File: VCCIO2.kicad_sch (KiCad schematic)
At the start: 19 parts, among them J5001 Micro_SD_Card_Det1, U3001 rv1126/rv1109

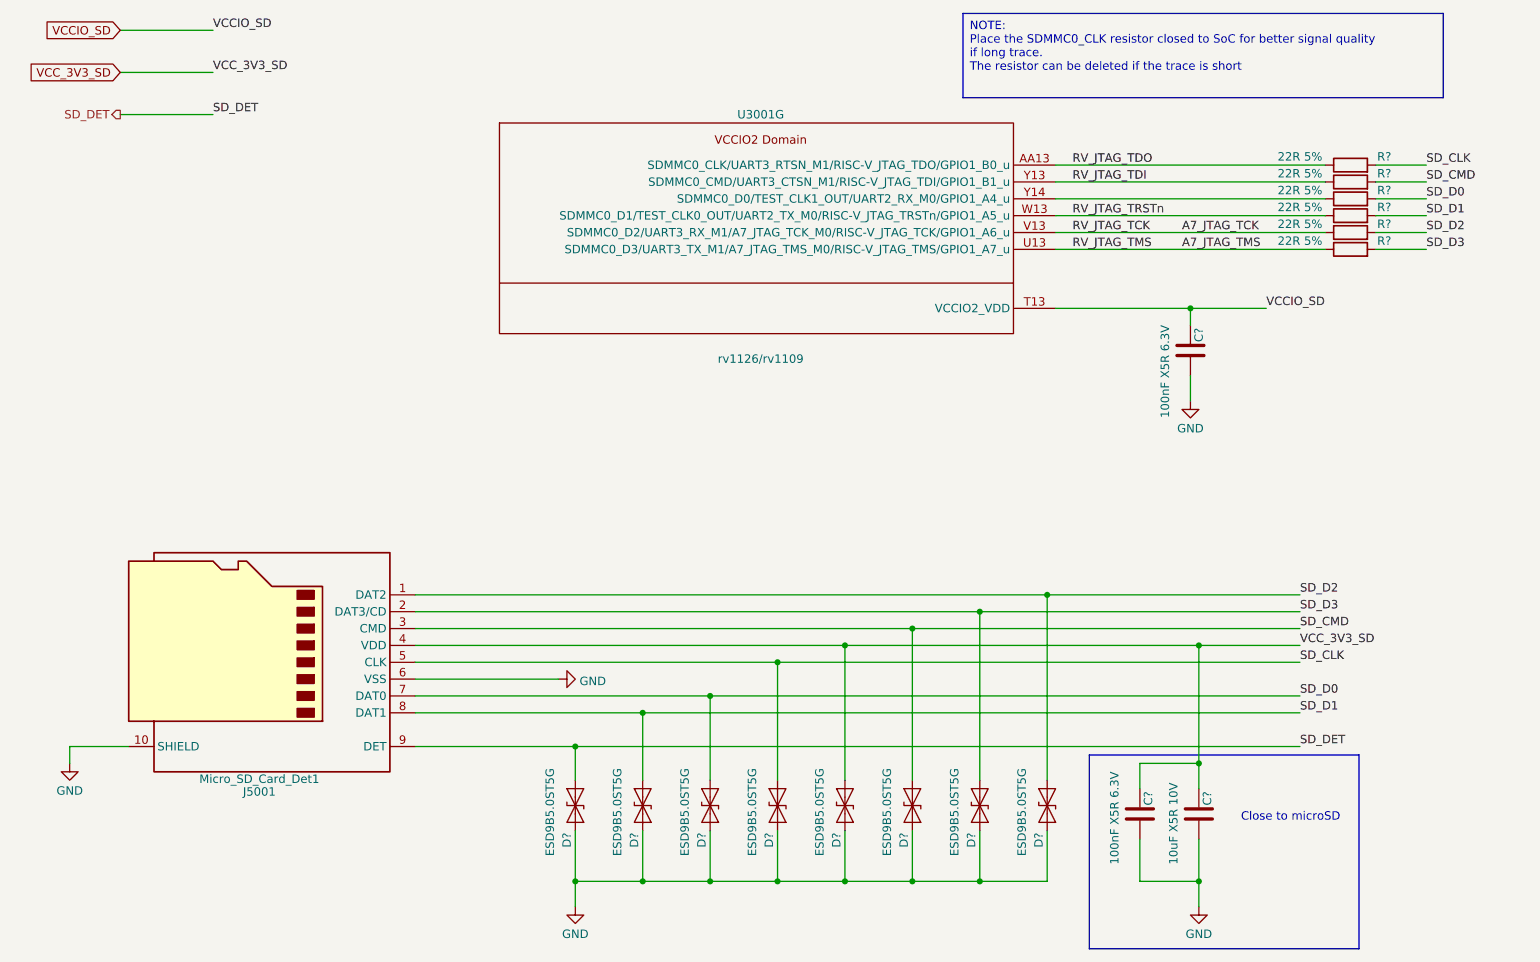
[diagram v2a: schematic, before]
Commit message: move DDR power decoupling capacitors into DDR4 Sheet
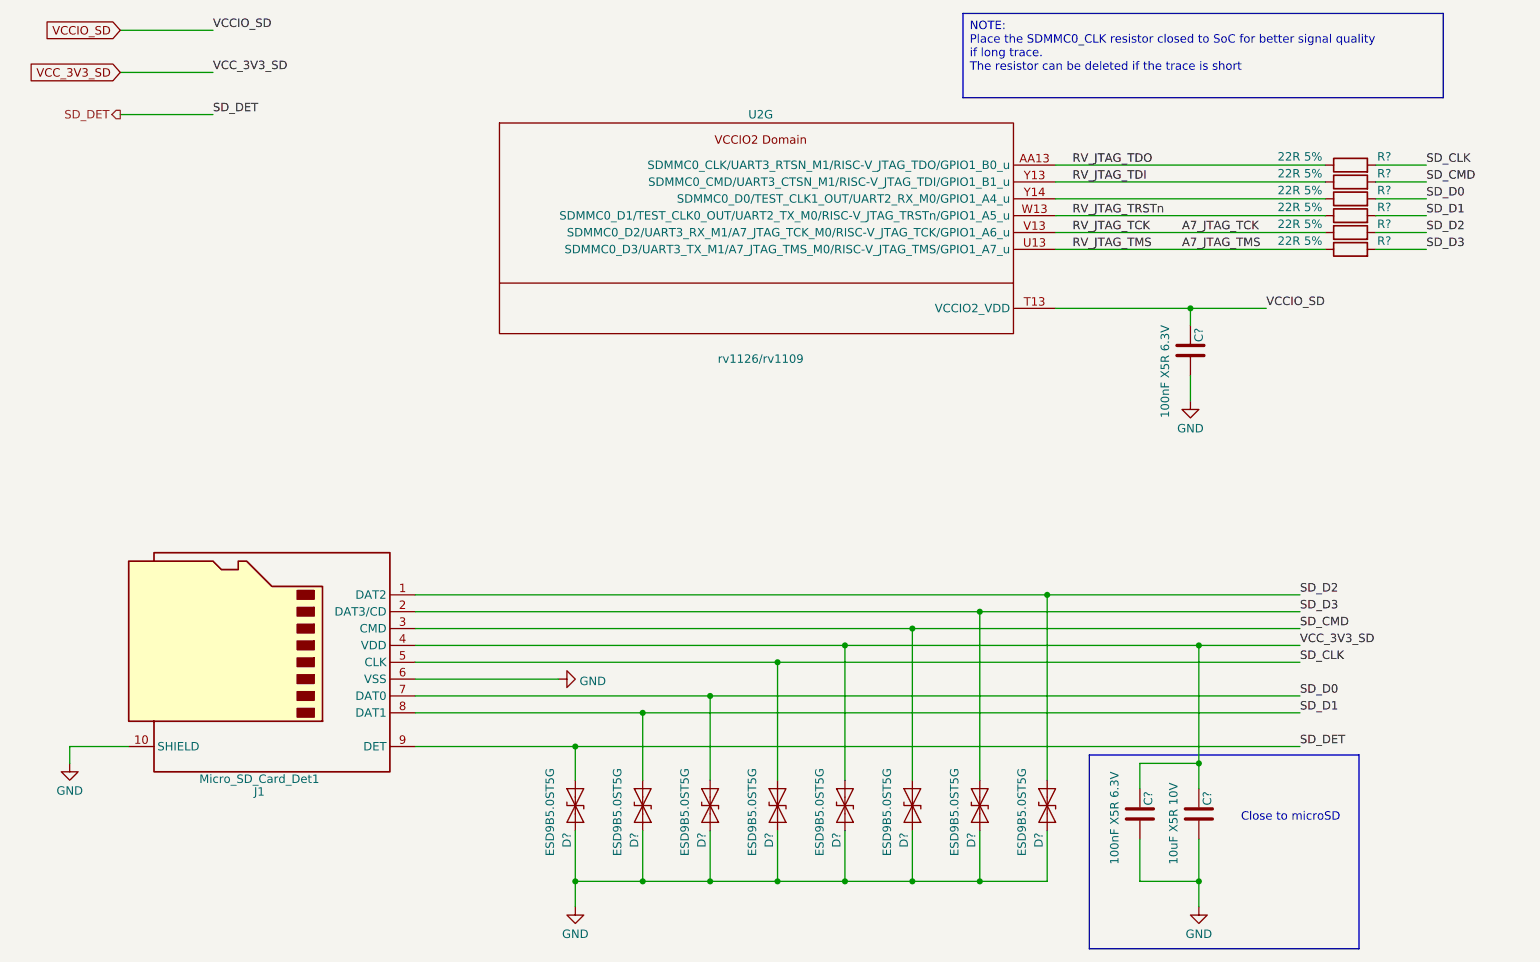
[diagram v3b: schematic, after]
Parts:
- renumbered J5001 to J1, U3001 to U2
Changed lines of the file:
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@@
         )
         (path "/e3b58043-16a3-43c8-9fad-9c9784eebfa4/4417415c-26f1-4372-988d-9fdf1c116b4b"
-          (reference "C5003") (unit 1)
+          (reference "C16") (unit 1)
         )
       )
@@
         )
         (path "/e3b58043-16a3-43c8-9fad-9c9784eebfa4/4417415c-26f1-4372-988d-9fdf1c116b4b"
-          (reference "D5003") (unit 1)
+          (reference "D3") (unit 1)
         )
       )
@@
         )
         (path "/e3b58043-16a3-43c8-9fad-9c9784eebfa4/4417415c-26f1-4372-988d-9fdf1c116b4b"
-          (reference "D5001") (unit 1)
+          (reference "D1") (unit 1)
         )
       )
@@
         )
         (path "/e3b58043-16a3-43c8-9fad-9c9784eebfa4/4417415c-26f1-4372-988d-9fdf1c116b4b"
-          (reference "C5002") (unit 1)
+          (reference "C15") (unit 1)
         )
       )
@@
   (symbol (lib_id "power:GND") (at 193.04 153.67 0) (unit 1)
     (in_bom yes) (on_board yes) (dnp no) (fields_autoplaced)
-    (property "Reference" "#PWR05005" (at 193.04 160.02 0)
+    (property "Reference" "#PWR019" (at 193.04 160.02 0)
       (effects (font (size 1.27 1.27)) hide)
     )
@@
       (project "leaf"
         (path "/e3b58043-16a3-43c8-9fad-9c9784eebfa4/4417415c-26f1-4372-988d-9fdf1c116b4b"
-          (reference "#PWR05005") (unit 1)
+          (reference "#PWR019") (unit 1)
         )
       )
@@
   (symbol (lib_id "power:GND") (at 96.52 119.38 90) (unit 1)
     (in_bom yes) (on_board yes) (dnp no) (fields_autoplaced)
-    (property "Reference" "#PWR05002" (at 102.87 119.38 0)
+    (property "Reference" "#PWR016" (at 102.87 119.38 0)
       (effects (font (size 1.27 1.27)) hide)
     )
@@
       (project "leaf"
         (path "/e3b58043-16a3-43c8-9fad-9c9784eebfa4/4417415c-26f1-4372-988d-9fdf1c116b4b"
-          (reference "#PWR05002") (unit 1)
+          (reference "#PWR016") (unit 1)
         )
       )
@@
         )
         (path "/e3b58043-16a3-43c8-9fad-9c9784eebfa4/4417415c-26f1-4372-988d-9fdf1c116b4b"
-          (reference "D5005") (unit 1)
+          (reference "D5") (unit 1)
         )
       )
@@
         )
         (path "/e3b58043-16a3-43c8-9fad-9c9784eebfa4/4417415c-26f1-4372-988d-9fdf1c116b4b"
-          (reference "D5004") (unit 1)
+          (reference "D4") (unit 1)
         )
       )
@@
         )
         (path "/e3b58043-16a3-43c8-9fad-9c9784eebfa4/4417415c-26f1-4372-988d-9fdf1c116b4b"
-          (reference "C5001") (unit 1)
+          (reference "C14") (unit 1)
         )
       )
@@
   (symbol (lib_id "Connector:Micro_SD_Card_Det1") (at 52.07 116.84 0) (mirror y) (unit 1)
     (in_bom yes) (on_board yes) (dnp no)
-    (property "Reference" "J5001" (at 51.435 136.3599 0)
+    (property "Reference" "J1" (at 51.435 136.3599 0)
       (effects (font (size 1.27 1.27)))
     )
@@
       (project "leaf"
         (path "/e3b58043-16a3-43c8-9fad-9c9784eebfa4/4417415c-26f1-4372-988d-9fdf1c116b4b"
-          (reference "J5001") (unit 1)
+          (reference "J1") (unit 1)
         )
       )
@@
         )
         (path "/e3b58043-16a3-43c8-9fad-9c9784eebfa4/4417415c-26f1-4372-988d-9fdf1c116b4b"
-          (reference "D5006") (unit 1)
+          (reference "D6") (unit 1)
         )
       )
@@
         )
         (path "/e3b58043-16a3-43c8-9fad-9c9784eebfa4/4417415c-26f1-4372-988d-9fdf1c116b4b"
-          (reference "D5008") (unit 1)
+          (reference "D8") (unit 1)
         )
       )
@@
         )
         (path "/e3b58043-16a3-43c8-9fad-9c9784eebfa4/4417415c-26f1-4372-988d-9fdf1c116b4b"
-          (reference "R5006") (unit 1)
+          (reference "R12") (unit 1)
         )
       )
@@
   (symbol (lib_id "CPU_Rockchip:rv1126_rv1109") (at 127 59.69 0) (unit 7)
     (in_bom yes) (on_board yes) (dnp no)
-    (property "Reference" "U3001" (at 127 34.29 0)
+    (property "Reference" "U2" (at 127 34.29 0)
       (effects (font (size 1.27 1.27)))
     )
@@
       (project "leaf"
         (path "/e3b58043-16a3-43c8-9fad-9c9784eebfa4/4417415c-26f1-4372-988d-9fdf1c116b4b"
-          (reference "U3001") (unit 7)
+          (reference "U2") (unit 7)
         )
       )
@@
         )
         (path "/e3b58043-16a3-43c8-9fad-9c9784eebfa4/4417415c-26f1-4372-988d-9fdf1c116b4b"
-          (reference "R5003") (unit 1)
+          (reference "R9") (unit 1)
         )
       )
@@
         )
         (path "/e3b58043-16a3-43c8-9fad-9c9784eebfa4/4417415c-26f1-4372-988d-9fdf1c116b4b"
-          (reference "D5007") (unit 1)
+          (reference "D7") (unit 1)
         )
       )
@@
         )
         (path "/e3b58043-16a3-43c8-9fad-9c9784eebfa4/4417415c-26f1-4372-988d-9fdf1c116b4b"
-          (reference "D5002") (unit 1)
+          (reference "D2") (unit 1)
         )
       )
@@
         )
         (path "/e3b58043-16a3-43c8-9fad-9c9784eebfa4/4417415c-26f1-4372-988d-9fdf1c116b4b"
-          (reference "R5005") (unit 1)
+          (reference "R11") (unit 1)
         )
       )
@@
         )
         (path "/e3b58043-16a3-43c8-9fad-9c9784eebfa4/4417415c-26f1-4372-988d-9fdf1c116b4b"
-          (reference "R5002") (unit 1)
+          (reference "R8") (unit 1)
         )
       )
@@
   (symbol (lib_id "power:GND") (at 99.06 153.67 0) (unit 1)
     (in_bom yes) (on_board yes) (dnp no) (fields_autoplaced)
-    (property "Reference" "#PWR05003" (at 99.06 160.02 0)
+    (property "Reference" "#PWR017" (at 99.06 160.02 0)
       (effects (font (size 1.27 1.27)) hide)
     )
@@
       (project "leaf"
         (path "/e3b58043-16a3-43c8-9fad-9c9784eebfa4/4417415c-26f1-4372-988d-9fdf1c116b4b"
-          (reference "#PWR05003") (unit 1)
+          (reference "#PWR017") (unit 1)
         )
       )
@@
   (symbol (lib_id "power:GND") (at 22.86 132.08 0) (unit 1)
     (in_bom yes) (on_board yes) (dnp no) (fields_autoplaced)
-    (property "Reference" "#PWR05001" (at 22.86 138.43 0)
+    (property "Reference" "#PWR015" (at 22.86 138.43 0)
       (effects (font (size 1.27 1.27)) hide)
     )
@@
       (project "leaf"
         (path "/e3b58043-16a3-43c8-9fad-9c9784eebfa4/4417415c-26f1-4372-988d-9fdf1c116b4b"
-          (reference "#PWR05001") (unit 1)
+          (reference "#PWR015") (unit 1)
         )
       )
@@
         )
         (path "/e3b58043-16a3-43c8-9fad-9c9784eebfa4/4417415c-26f1-4372-988d-9fdf1c116b4b"
-          (reference "R5004") (unit 1)
+          (reference "R10") (unit 1)
         )
       )
@@
   (symbol (lib_id "power:GND") (at 191.77 77.47 0) (unit 1)
     (in_bom yes) (on_board yes) (dnp no) (fields_autoplaced)
-    (property "Reference" "#PWR05004" (at 191.77 83.82 0)
+    (property "Reference" "#PWR018" (at 191.77 83.82 0)
       (effects (font (size 1.27 1.27)) hide)
     )
@@
       (project "leaf"
         (path "/e3b58043-16a3-43c8-9fad-9c9784eebfa4/4417415c-26f1-4372-988d-9fdf1c116b4b"
-          (reference "#PWR05004") (unit 1)
+          (reference "#PWR018") (unit 1)
         )
       )
@@
         )
         (path "/e3b58043-16a3-43c8-9fad-9c9784eebfa4/4417415c-26f1-4372-988d-9fdf1c116b4b"
-          (reference "R5001") (unit 1)
-        )
-      )
+          (reference "R7") (unit 1)
+        )
+      )

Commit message: remove all warnings
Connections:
- net A7_JTAG_TCK renamed JTAG_TCK
- net A7_JTAG_TMS renamed JTAG_TMS
- net RV_JTAG_TDI renamed JTAG_TDI
- net RV_JTAG_TDO renamed JTAG_TDO
- net RV_JTAG_TRSTn renamed JTAG_~{TRST}
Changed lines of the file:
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@@
     (effects (font (size 1.27 1.27)) (justify left bottom))
   )
-  (label "A7_JTAG_TMS" (at 190.5 54.61 0) (fields_autoplaced)
-    (effects (font (size 1.27 1.27)) (justify left bottom))
-  )
-  (label "RV_JTAG_TRSTn" (at 173.99 49.53 0) (fields_autoplaced)
+  (label "JTAG_~{TRST}" (at 173.99 49.53 0) (fields_autoplaced)
     (effects (font (size 1.27 1.27)) (justify left bottom))
   )
@@
     (effects (font (size 1.27 1.27)) (justify left bottom))
   )
-  (label "RV_JTAG_TCK" (at 173.99 52.07 0) (fields_autoplaced)
+  (label "JTAG_TCK" (at 173.99 52.07 0) (fields_autoplaced)
     (effects (font (size 1.27 1.27)) (justify left bottom))
   )
-  (label "RV_JTAG_TDI" (at 173.99 44.45 0) (fields_autoplaced)
+  (label "JTAG_TDI" (at 173.99 44.45 0) (fields_autoplaced)
     (effects (font (size 1.27 1.27)) (justify left bottom))
   )
@@
     (effects (font (size 1.27 1.27)) (justify left bottom))
   )
-  (label "RV_JTAG_TMS" (at 173.99 54.61 0) (fields_autoplaced)
+  (label "JTAG_TMS" (at 173.99 54.61 0) (fields_autoplaced)
     (effects (font (size 1.27 1.27)) (justify left bottom))
   )
@@
     (effects (font (size 1.27 1.27)) (justify left bottom))
   )
-  (label "RV_JTAG_TDO" (at 173.99 41.91 0) (fields_autoplaced)
+  (label "JTAG_TDO" (at 173.99 41.91 0) (fields_autoplaced)
     (effects (font (size 1.27 1.27)) (justify left bottom))
   )
@@
     (effects (font (size 1.27 1.27)) (justify left bottom))
   )
-  (label "A7_JTAG_TCK" (at 190.5 52.07 0) (fields_autoplaced)
-    (effects (font (size 1.27 1.27)) (justify left bottom))
-  )

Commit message: added README and license
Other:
- company: Qingdao IotPi Information Technology -> Yang Hongbo
- title: Leaf RV1126 RK809 SDCard -> Leaf RV1126
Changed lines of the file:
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@@
   (paper "A4")
   (title_block
-    (title "Leaf RV1126 RK809 SDCard")
-    (date "2023-02-25")
+    (title "Leaf RV1126")
+    (date "2023-06-07")
     (rev "1")
-    (company "Qingdao IotPi Information Technology")
+    (company "Yang Hongbo")
+    (comment 1 "License: CC BY-SA")
   )
   (junction (at 160.02 149.86) (diameter 0) (color 0 0 0 0)

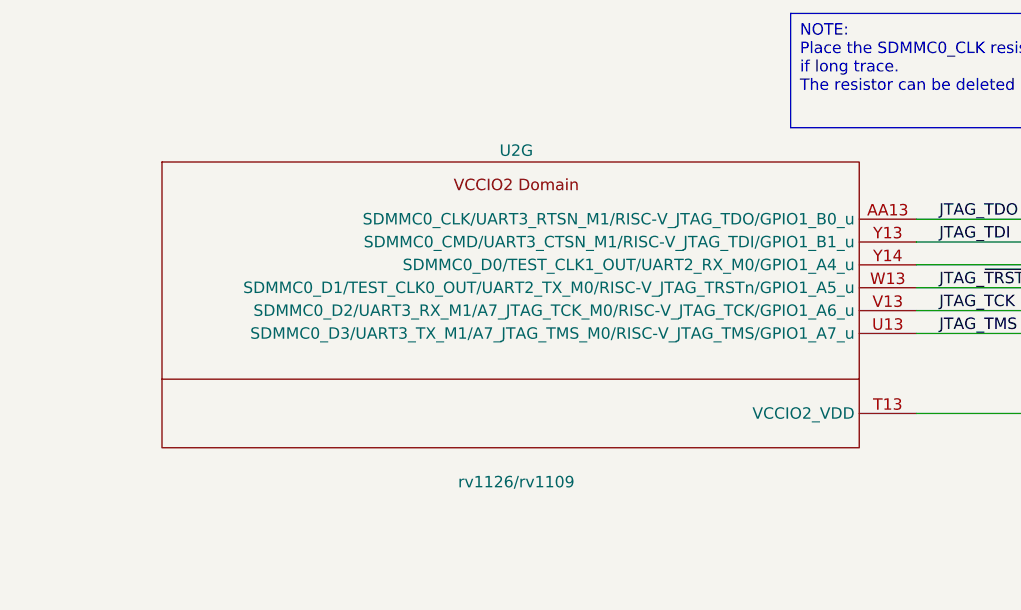
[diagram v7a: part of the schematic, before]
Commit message: replaced Leaf specified symbols with unified iotpi symbols
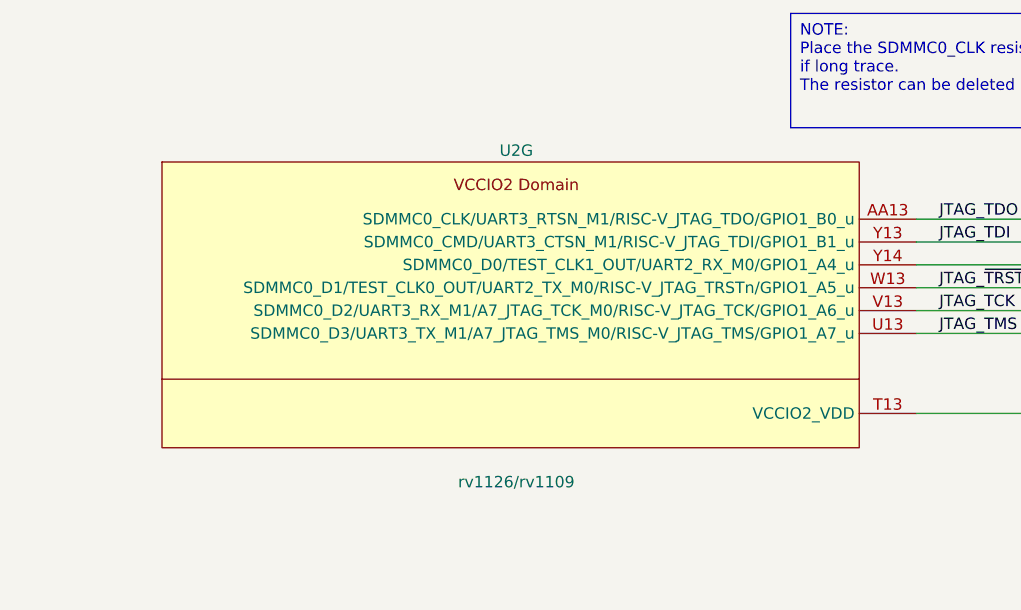
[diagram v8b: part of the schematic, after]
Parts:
- U2: symbol CPU_Rockchip:rv1126_rv1109 -> IotPi_CPU_Rockchip:rv1126_rv1109
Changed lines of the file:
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@@
       (effects (font (size 1.27 1.27)) hide)
     )
-    (property "Datasheet" "" (at 52.07 114.3 0)
+    (property "Datasheet" "https://datasheet.lcsc.com/lcsc/2110151630_XKB-Connectivity-XKTF-015-N_C381082.pdf" (at 52.07 114.3 0)
       (effects (font (size 1.27 1.27)) hide)
     )
@@
     )
   )
-  (symbol (lib_id "CPU_Rockchip:rv1126_rv1109") (at 127 59.69 0) (unit 7)
+  (symbol (lib_id "IotPi_CPU_Rockchip:rv1126_rv1109") (at 127 59.69 0) (unit 7)
     (in_bom yes) (on_board yes) (dnp no)
     (property "Reference" "U2" (at 127 34.29 0)
@@
       (effects (font (size 1.27 1.27)))
     )
-    (property "Footprint" "Rockchip_SoC:Rockchip_RV1126_FCCSP409LD_14.0x14.0mm" (at 144.78 93.98 0)
+    (property "Footprint" "Rockchip_SoC:Rockchip_RV1126_FCCSP409LD_14.0x14.0mm" (at 158.75 106.68 0)
       (effects (font (size 1.27 1.27)) hide)
     )
-    (property "Datasheet" "" (at 144.78 93.98 0)
+    (property "Datasheet" "" (at 158.75 106.68 0)
       (effects (font (size 1.27 1.27)) hide)
     )
